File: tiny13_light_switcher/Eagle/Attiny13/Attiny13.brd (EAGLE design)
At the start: 80 x 80 mm, 35 parts, among them J1 USB_A_SMT_MALE, Q4 2N7000, Q5 2N7000, Q6 2N7000, U1 ATTiny13, U2 ATTiny85

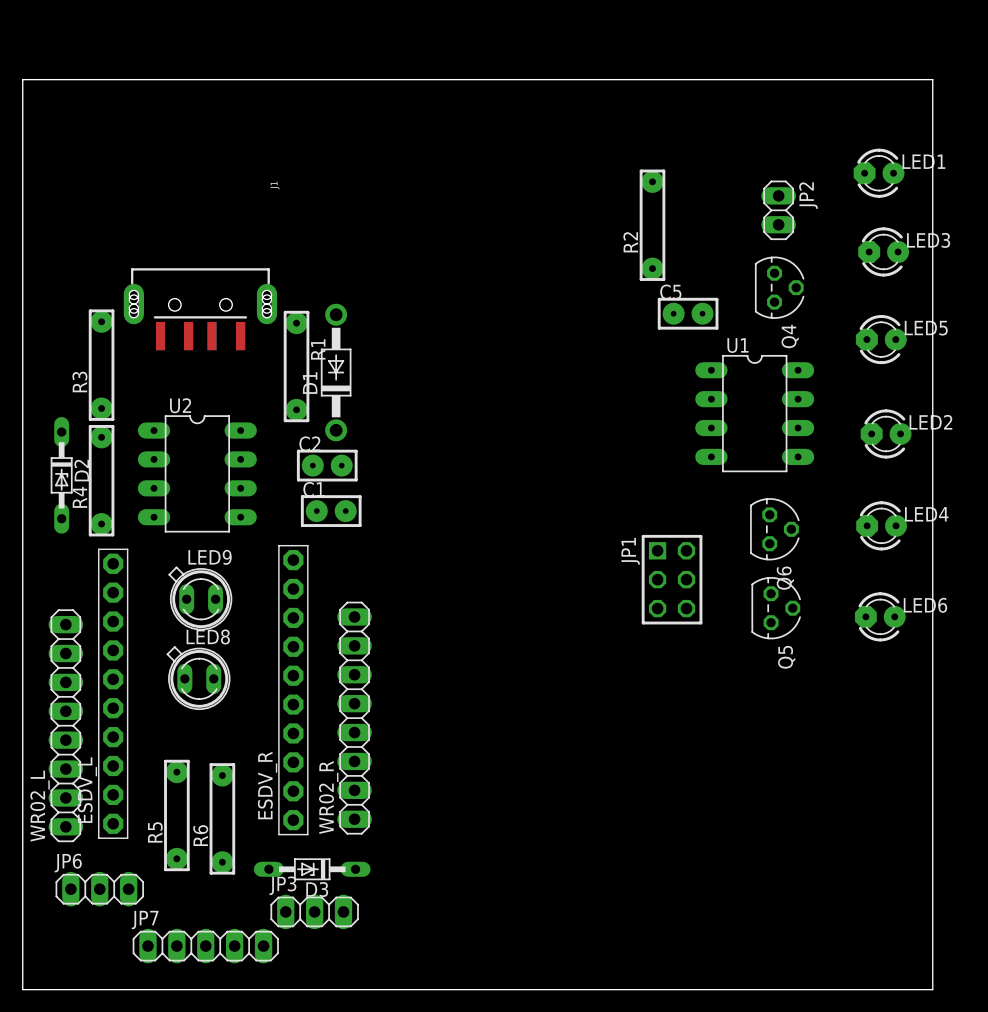
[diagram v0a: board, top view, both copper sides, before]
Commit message: Change USB connector.
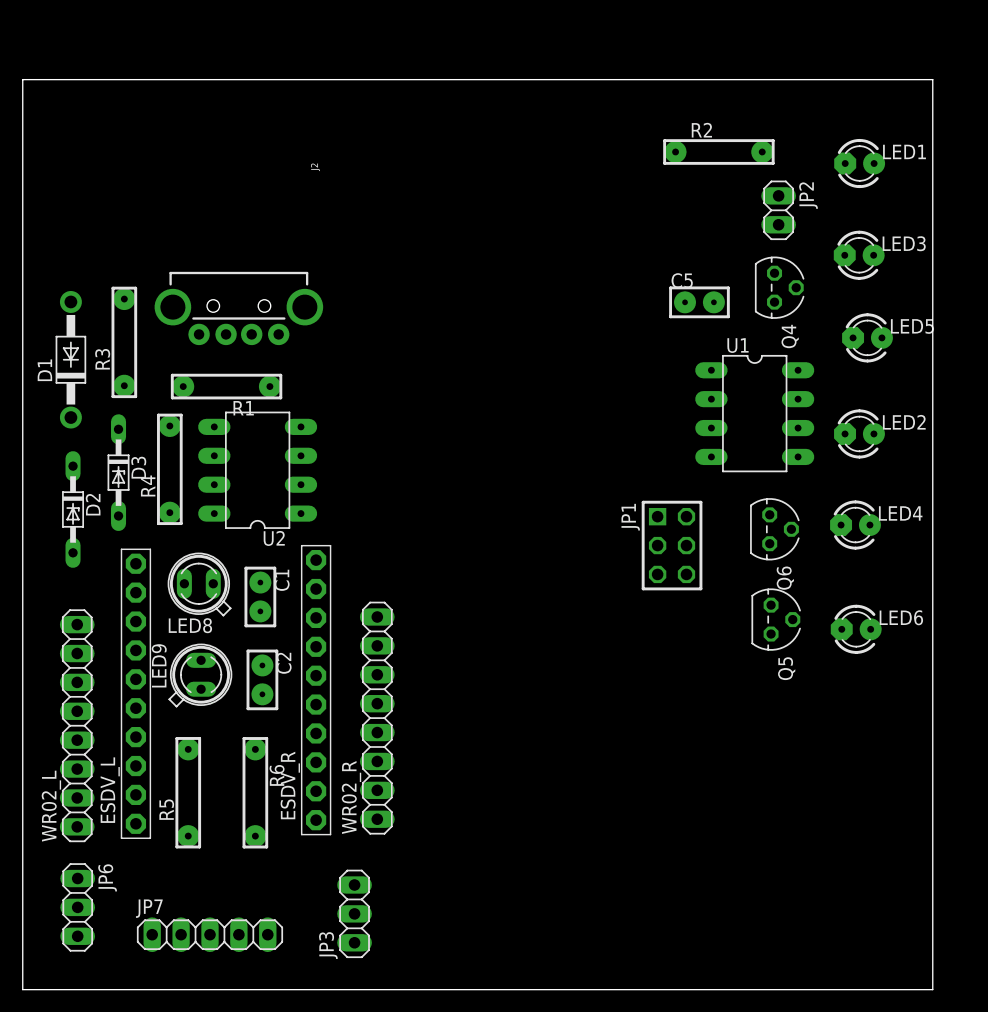
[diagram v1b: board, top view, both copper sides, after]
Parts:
- removed J1: USB_A_SMT_MALE, SparkFun-Connectors:USB-A-SMT-MALE
- added J2: USB_A_PTH_MALE, SparkFun-Connectors:USB-A-H
- JP2: value VDD -> PWR_SPLY
- moved D3 38.8 mm to (8.42, 45.5), turned to 270 degrees
- moved D1 23.3 mm to (4.23, 55.4)
- moved C2 19.7 mm to (21.1, 27.2), turned to 270 degrees
- moved C1 9.79 mm to (20.9, 34.5), turned to 270 degrees
- moved R2 8.69 mm to (61.2, 73.6), turned to 0 degrees
- moved LED8 8.36 mm to (15.5, 35.7), turned to 180 degrees
- moved LED9 6.64 mm to (15.7, 27.7), turned to 90 degrees
- moved R1 6.40 mm to (17.9, 53.0), turned to 180 degrees
- moved R4 6.08 mm to (12.9, 45.7)
- moved U2 5.31 mm to (20.6, 45.7), turned to 90 degrees
- moved R6 3.70 mm to (20.4, 17.3), turned to 270 degrees
- moved JP3 3.51 mm to (29.2, 6.66), turned to 90 degrees
- moved D2 3.16 mm to (4.42, 42.2)
- moved JP1 3.00 mm to (57.1, 39.0)
- moved R3 2.83 mm to (8.93, 56.9)
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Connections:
- new net AGND: C1.1, C2.1, D2.A, D3.A, ESDV_L.9, ESDV_R.1, ESDV_R.9, J2.GND, JP7.3, R5.1, R6.2, U2.4, WR02_R.1
- net GND: no longer C1.1, C2.1, D2.A, D3.A, ESDV_L.9, ESDV_R.1, ESDV_R.9, J1.GND1, JP7.3, R5.1, R6.2, U2.4, WR02_R.1
- net N$1: now also J2.VBUS; no longer J1.VBUS1
- net N$19: now also J2.D+; no longer J1.D+1
- net N$4: now also J2.D-; no longer J1.D-1

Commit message: Add pattern.
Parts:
- removed J2: USB_A_PTH_MALE, SparkFun-Connectors:USB-A-H
- added J1: USB_A_PTH_MALE, SparkFun-Connectors:USB-A-H
- added R7: R_LED16, MyLib:R_0.125W_3
- added R8: R_LED34, MyLib:R_0.125W_3
- added R9: R_LED25, MyLib:R_0.125W_3
- added USB1: USBA_RAW, MyParts:USBA_RAW
- moved D1 26.0 mm to (28.8, 46.6), turned to 270 degrees
- moved R3 20.5 mm to (19.1, 39.1), turned to 270 degrees
- moved LED9 15.4 mm to (12.3, 12.7), turned to 180 degrees
- moved LED8 14.3 mm to (12.5, 21.7)
- moved D3 13.0 mm to (16.8, 55.5), turned to 180 degrees
- moved D2 12.8 mm to (13.2, 51.6), turned to 180 degrees
- moved R4 12.2 mm to (22.9, 38.7)
- moved U2 10.0 mm to (10.7, 44.7)
- moved C1 8.06 mm to (13.9, 30.5)
- moved R1 6.40 mm to (24.0, 51.1), turned to 90 degrees
- moved JP3 6.35 mm to (23.3, 9.17), turned to 180 degrees
- moved WR02_L 4.73 mm to (3.71, 27.8), turned to 270 degrees
- moved WR02_R 3.99 mm to (31.6, 27.8), turned to 270 degrees
- moved R5 3.92 mm to (18.4, 17.7), turned to 270 degrees
- moved ESDV_L 3.77 mm to (6.25, 25.3), turned to 270 degrees
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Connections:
- new net N$30: LED1.A, LED6.A, R7.2
- new net N$31: LED3.A, LED4.A, R8.2
- new net N$32: LED2.A, LED5.A, R9.2
- net AGND: now also J1.GND, USB1.GND; no longer J2.GND
- net N$1: now also J1.VBUS, USB1.VBUS; no longer J2.VBUS
- net N$19: now also J1.D+, USB1.D+; no longer J2.D+
- net N$4: now also J1.D-, USB1.D-; no longer J2.D-
- net VCC: now also R7.1, R8.1, R9.1; no longer LED1.A, LED2.A, LED3.A, LED4.A, LED5.A, LED6.A

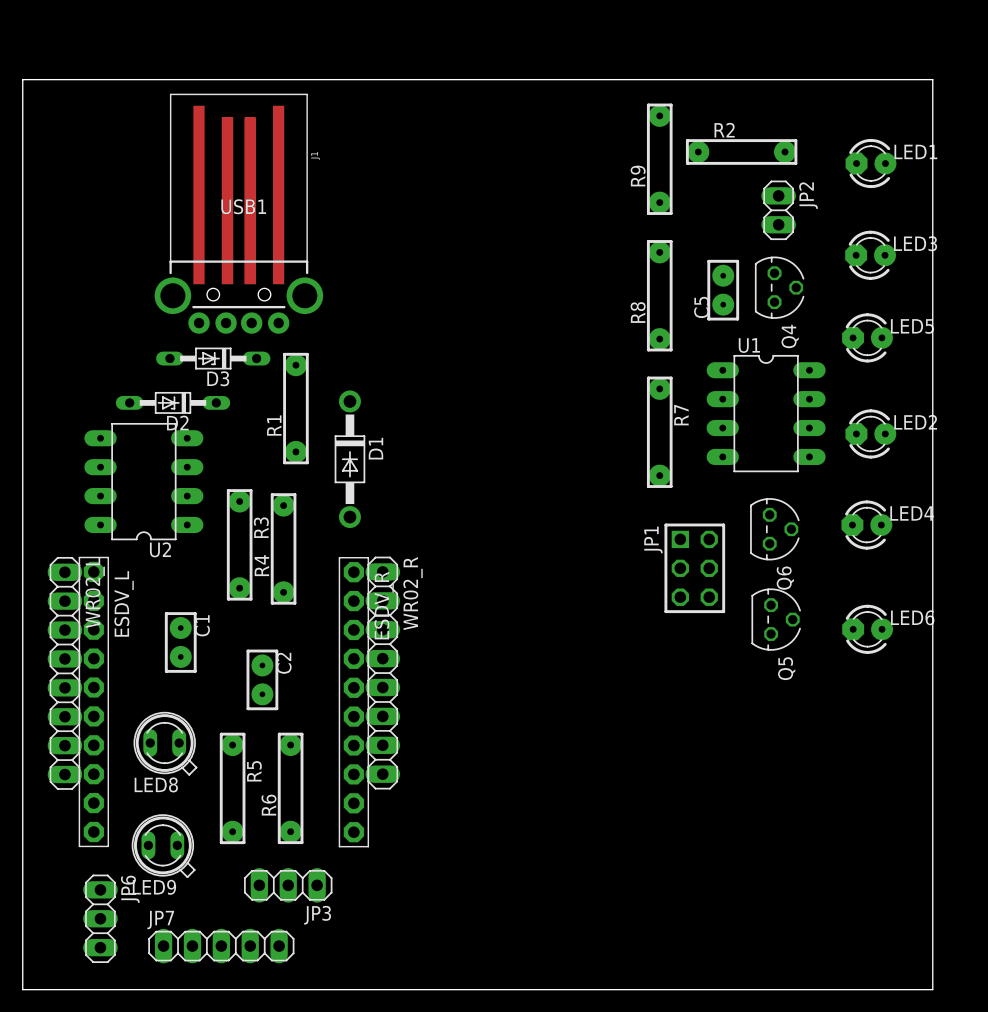
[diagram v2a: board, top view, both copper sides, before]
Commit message: Fix USB & parts layout.
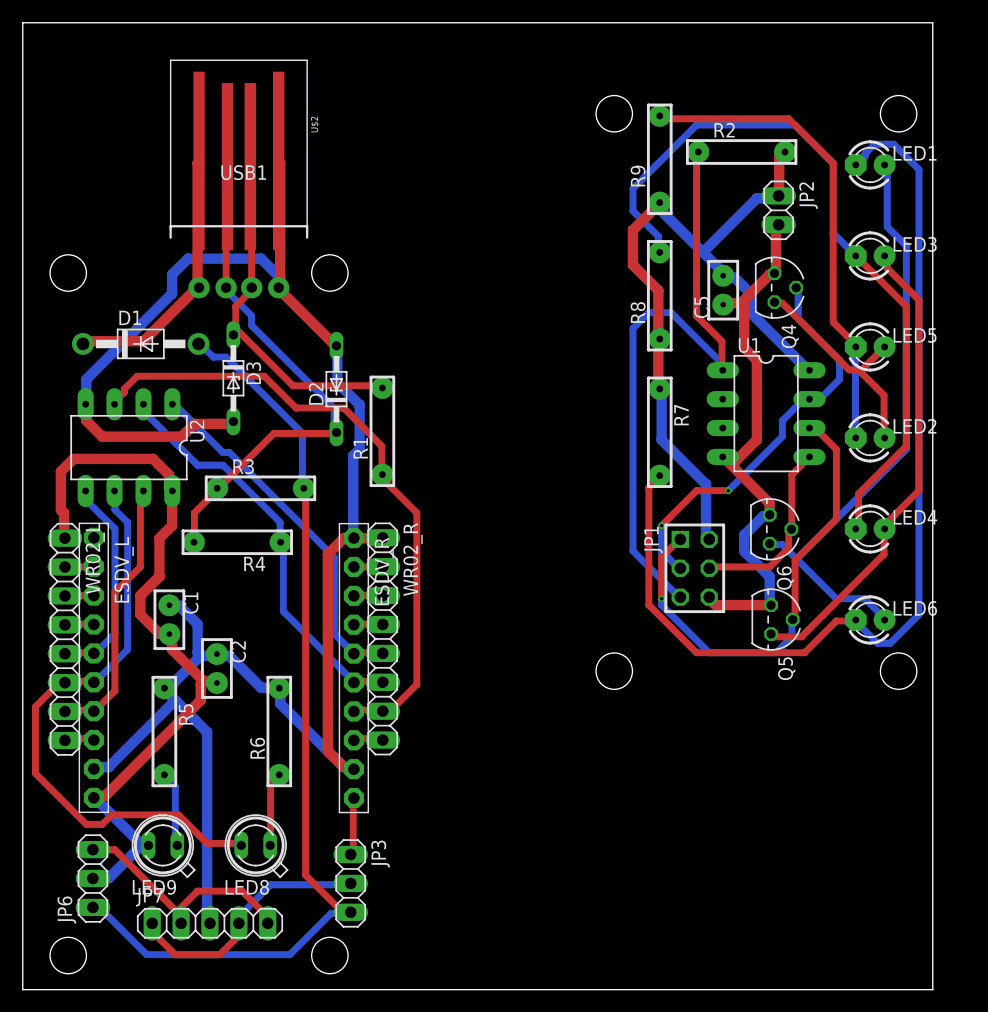
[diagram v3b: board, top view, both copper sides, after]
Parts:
- removed J1: USB_A_PTH_MALE, SparkFun-Connectors:USB-A-H
- added U$2: USB_MY_BREAKOUT, MyParts:USB_MY_BREAKOUT
- moved D1 21.0 mm to (10.4, 56.8), turned to 0 degrees
- moved D2 14.4 mm to (27.6, 52.8), turned to 90 degrees
- moved LED8 12.0 mm to (20.5, 12.7)
- moved R1 7.86 mm to (31.6, 49.1)
- moved R5 7.81 mm to (12.4, 22.7)
- moved JP3 5.49 mm to (28.8, 9.34), turned to 270 degrees
- moved R3 5.30 mm to (20.9, 44.1), turned to 0 degrees
- moved R6 5.10 mm to (22.6, 22.7)
- moved C2 4.12 mm to (17.1, 28.2)
- moved R4 4.11 mm to (18.9, 39.3), turned to 180 degrees
- moved JP6 3.60 mm to (6.17, 9.77), turned to 90 degrees
- moved U2 3.26 mm to (9.34, 47.6), turned to 180 degrees
- moved ESDV_L 3.00 mm to (6.25, 28.3)
- moved ESDV_R 3.00 mm to (29.1, 28.3)
- moved USB1 3.00 mm to (19.0, 75.0)
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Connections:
- net AGND: now also U$2.GND; no longer J1.GND
- net N$1: now also U$2.VBUS; no longer J1.VBUS
- net N$19: now also U$2.D+; no longer J1.D+
- net N$4: now also U$2.D-; no longer J1.D-
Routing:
- net AGND: track 0.00 -> 165.1 mm
- net N$30: track 0.00 -> 86.9 mm
- net VDD: track 0.00 -> 82.7 mm
- net VCC: track 0.00 -> 67.1 mm
- net +5V: track 0.00 -> 66.8 mm
- net N$31: track 0.00 -> 64.7 mm
- net N$7: track 0.00 -> 56.5 mm
- net N$11: track 0.00 -> 56.1 mm
- net N$5: track 0.00 -> 52.4 mm
- net N$15: track 0.00 -> 51.9 mm
- net GND: track 0.00 -> 49.4 mm
- net N$4: track 0.00 -> 45.5 mm
- net N$32: track 0.00 -> 42.0 mm
- net N$10: track 0.00 -> 41.8 mm
- net N$8: track 0.00 -> 41.5 mm, vias 0 -> 1
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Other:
- board size 80 x 80 mm -> 80 x 85 mm

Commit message: Change capacitor package.
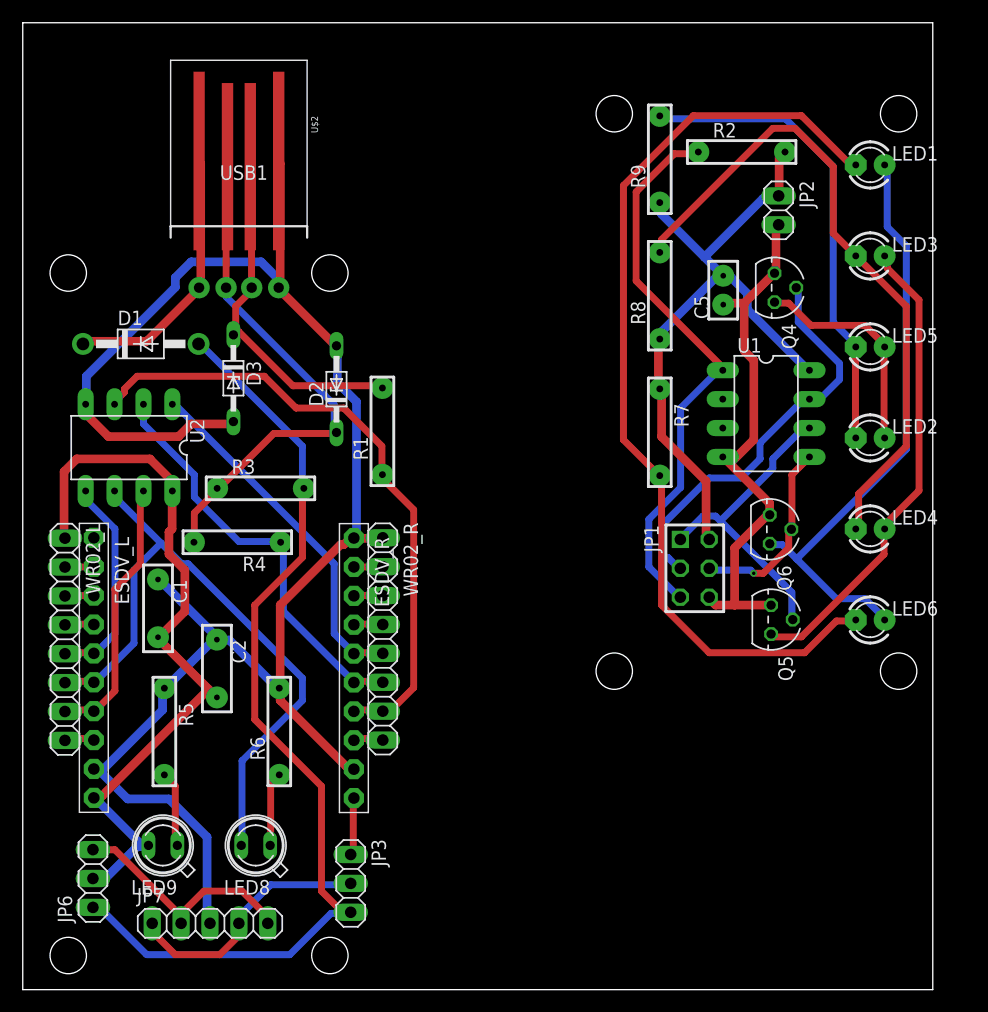
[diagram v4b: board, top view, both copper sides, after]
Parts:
- C1, C2: device MyLib:CAP_DIP_1 -> MyLib:CAP_DIP_2
- moved C1 1.41 mm to (11.9, 33.5)
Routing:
- net N$8: track 41.5 -> 27.6 mm, vias 1 -> 0
- net AGND: track 165.1 -> 157.5 mm
- net N$31: track 64.7 -> 58.3 mm
- net N$7: track 56.5 -> 50.2 mm
- net N$15: track 51.9 -> 58.1 mm
- net VCC: track 67.1 -> 61.3 mm
- net N$30: track 86.9 -> 83.1 mm
- net VDD: track 82.7 -> 85.6 mm
- net GND: track 49.4 -> 48.0 mm
- net +5V: track 66.8 -> 65.6 mm
- net N$3: track 36.0 -> 36.8 mm
- net N$6: track 16.5 -> 16.9 mm, vias 0 -> 1
- net N$2: vias 2 -> 0

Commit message: Resolve DRC & ERC.
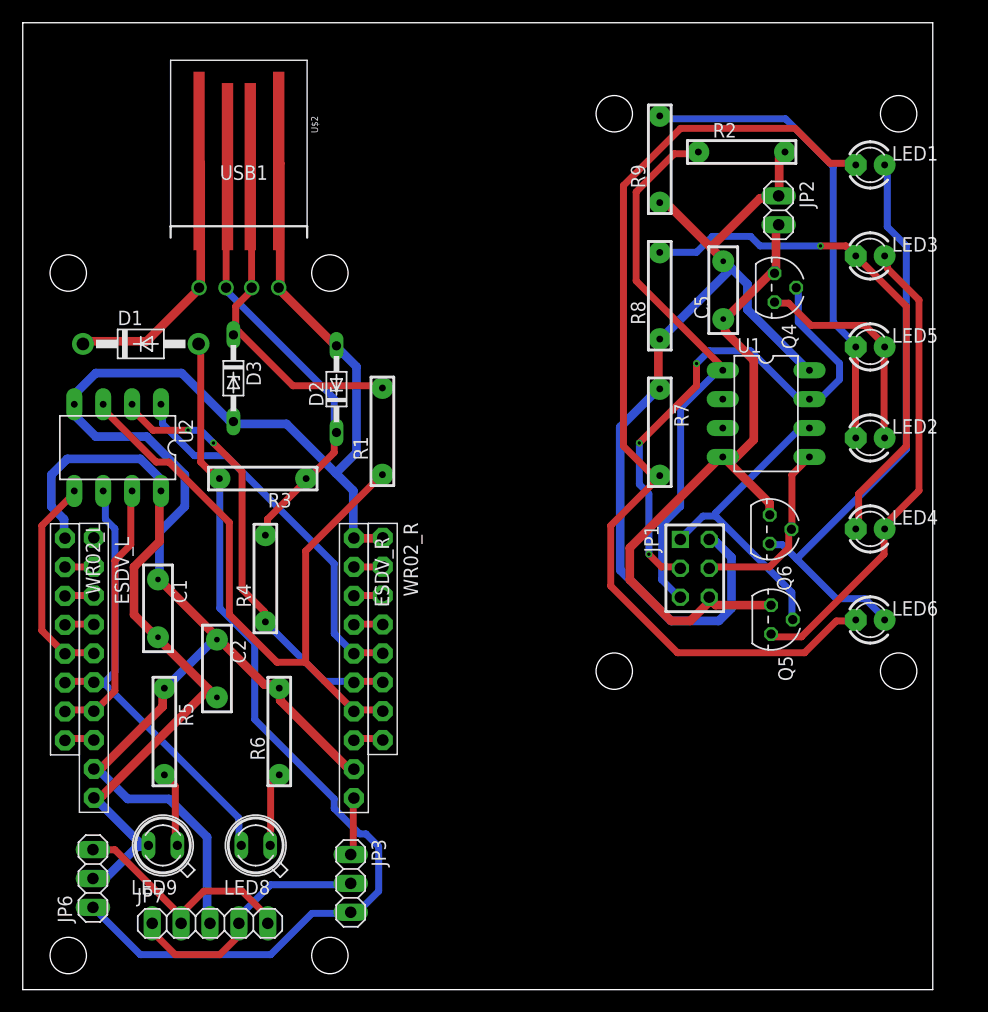
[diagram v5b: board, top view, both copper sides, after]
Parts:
- C5: device MyLib:CAP_DIP_1 -> MyLib:CAP_DIP_2
- U$2: value USB_MY_BREAKOUT -> USB_MY_BREAKOUTPATTERN2; device MyParts:USB_MY_BREAKOUT -> MyParts:USB_MY_BREAKOUT2
- WR02_L, WR02_R: device pinhead:1X08 -> adafruit:1X08-BIG
- moved R4 4.03 mm to (21.3, 36.1), turned to 90 degrees
- moved U2 1.00 mm to (8.34, 47.6)
- moved R3 0.88 mm to (21.1, 44.9), turned to 180 degrees
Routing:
- net VCC: track 61.3 -> 83.5 mm
- net N$15: track 58.1 -> 40.6 mm
- net GND: track 48.0 -> 62.5 mm
- net N$31: track 58.3 -> 46.3 mm, vias 0 -> 1
- net N$2: track 36.1 -> 47.6 mm, vias 0 -> 3
- net N$4: track 45.5 -> 39.3 mm
- net N$30: track 83.1 -> 87.9 mm
- net N$11: track 55.9 -> 60.3 mm
- net AGND: track 157.5 -> 153.2 mm
- net N$3: track 36.8 -> 39.1 mm, vias 0 -> 2
- net N$12: track 31.2 -> 33.2 mm
- net VDD: track 85.6 -> 84.3 mm
- net N$7: track 50.2 -> 49.2 mm
- net +5V: track 65.6 -> 66.4 mm
- net N$6: track 16.9 -> 16.5 mm, vias 1 -> 0

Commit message: Auto Routing OK.
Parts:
- moved C1 3.61 mm to (13.9, 36.5)
- moved R1 3.61 mm to (29.6, 52.1)
- moved D2 2.24 mm to (25.6, 53.8)
- moved R5 2.00 mm to (12.4, 24.7)
- moved U2 1.00 mm to (9.34, 47.6)
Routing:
- net +5V: track 66.4 -> 72.1 mm
- net N$11: track 60.3 -> 54.6 mm
- net N$3: track 39.1 -> 36.2 mm, vias 2 -> 0
- net N$19: track 30.8 -> 28.1 mm
- net N$13: track 6.66 -> 8.66 mm
- net N$12: track 33.2 -> 31.2 mm
- net N$4: track 39.3 -> 37.6 mm
- net N$15: track 40.6 -> 41.6 mm
- net AGND: track 153.2 -> 152.4 mm
- net VDD: track 84.3 -> 85.0 mm, vias 0 -> 1

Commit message: Fix Wiring.
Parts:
- moved Q6 16.3 mm to (49.7, 43.5)
- moved C5 16.3 mm to (45.6, 64.5)
- moved JP1 16.3 mm to (43.1, 40.0)
- moved JP2 16.3 mm to (50.5, 71.5)
- moved LED1 16.3 mm to (58.5, 75.5)
- moved LED2 16.3 mm to (58.5, 51.5)
- moved LED3 16.3 mm to (58.5, 67.5)
- moved LED4 16.3 mm to (58.5, 43.5)
- moved LED5 16.3 mm to (58.5, 59.5)
- moved LED6 16.3 mm to (58.5, 35.5)
- moved Q4 16.3 mm to (50.1, 64.7)
- moved R2 16.3 mm to (47.2, 76.6)
- moved R7 16.3 mm to (40.0, 52.0)
- moved R8 16.3 mm to (40.0, 64.0)
- moved R9 16.3 mm to (40.0, 76.0)
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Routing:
- net N$11: track 54.6 -> 56.9 mm, vias 0 -> 2
- net N$19: track 28.1 -> 29.5 mm
- net N$4: track 37.6 -> 39.0 mm
- net N$1: track 23.7 -> 25.0 mm
- net N$3: track 36.2 -> 37.3 mm
- net AGND: track 152.4 -> 153.2 mm
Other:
- board size 80 x 85 mm -> 63 x 83 mm
